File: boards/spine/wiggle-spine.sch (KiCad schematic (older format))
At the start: 0 parts

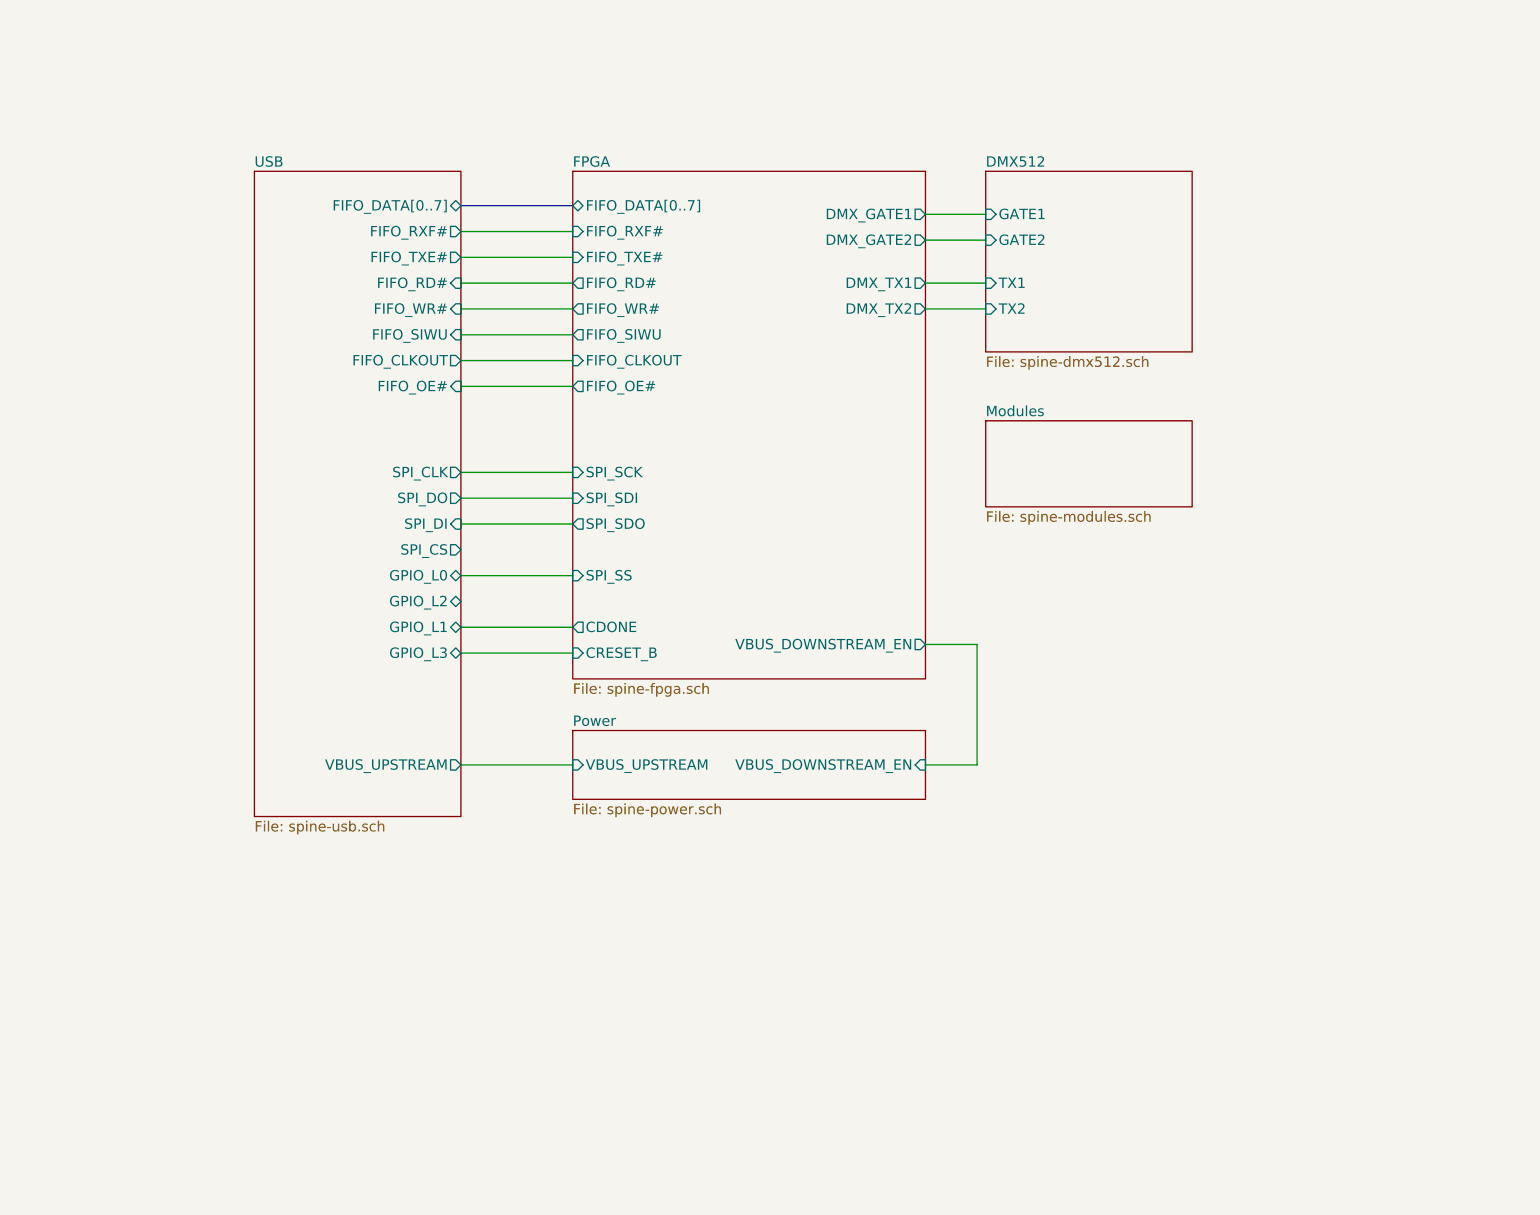
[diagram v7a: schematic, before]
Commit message: Clock generator, sync connectors, title blocks
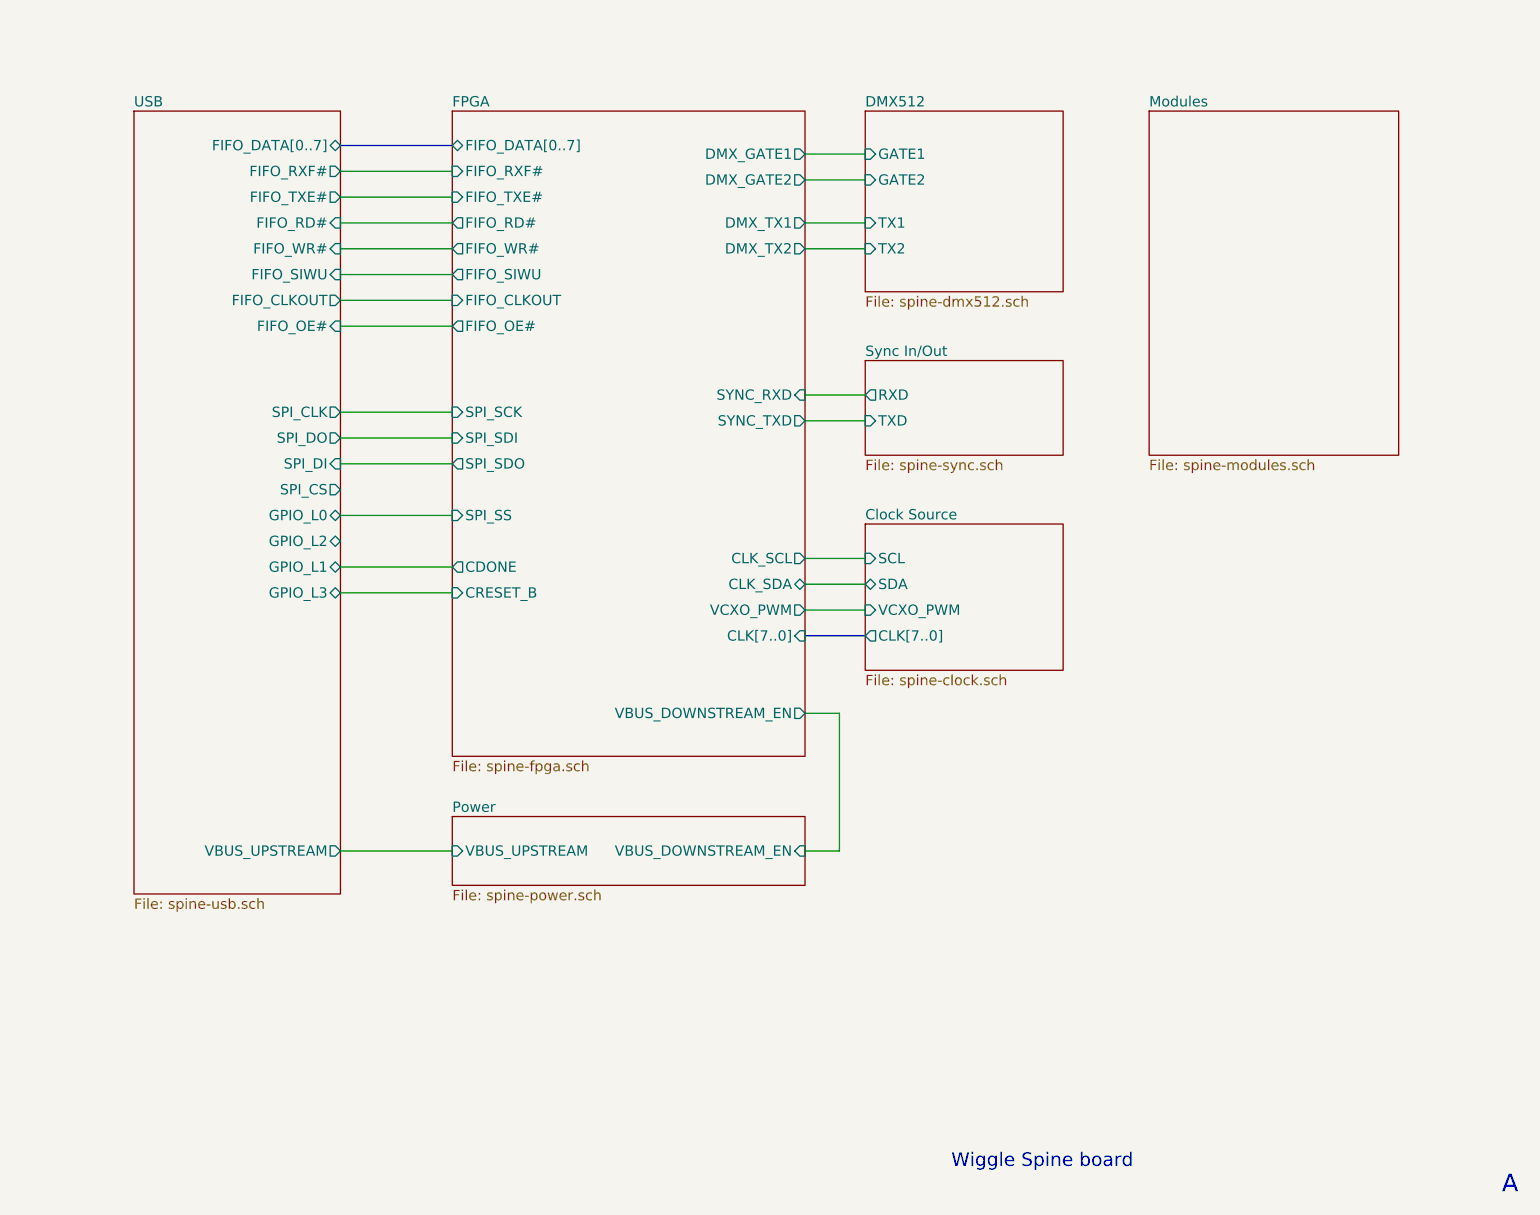
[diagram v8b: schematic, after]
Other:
- note added: "A"
- note added: "Wiggle Spine board"
